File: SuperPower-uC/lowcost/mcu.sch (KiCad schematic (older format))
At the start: 0 parts

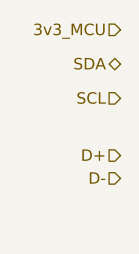
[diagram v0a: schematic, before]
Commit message: int pins and charging module
added Interrupt pins to the main sheet and finished the charging module sub sheet (with charger, fuel Gauge and power on int)
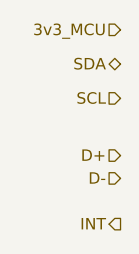
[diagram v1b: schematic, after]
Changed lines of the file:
@@
 Text HLabel 1300 1650 0    50   Input ~ 0
 D-
+Text HLabel 1300 1850 0    50   Output ~ 0
+INT
 $EndSCHEMATC

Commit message: relocated ftdi to connector sheet
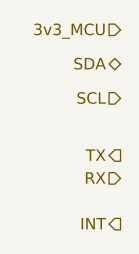
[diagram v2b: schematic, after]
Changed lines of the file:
@@
 Text HLabel 1300 1300 0    50   Input ~ 0
 SCL
-Text HLabel 1300 1550 0    50   Input ~ 0
-D+
+Text HLabel 1300 1550 0    50   Output ~ 0
+TX
 Text HLabel 1300 1650 0    50   Input ~ 0
-D-
+RX
 Text HLabel 1300 1850 0    50   Output ~ 0
 INT

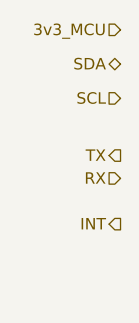
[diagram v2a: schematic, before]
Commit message: added ftdi and some cleanup
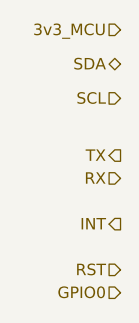
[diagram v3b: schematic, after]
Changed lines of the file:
@@
 Text HLabel 1300 1850 0    50   Output ~ 0
 INT
+Text HLabel 1300 2050 0    50   Input ~ 0
+RST
+Text HLabel 1300 2150 0    50   Input ~ 0
+GPIO0
 $EndSCHEMATC

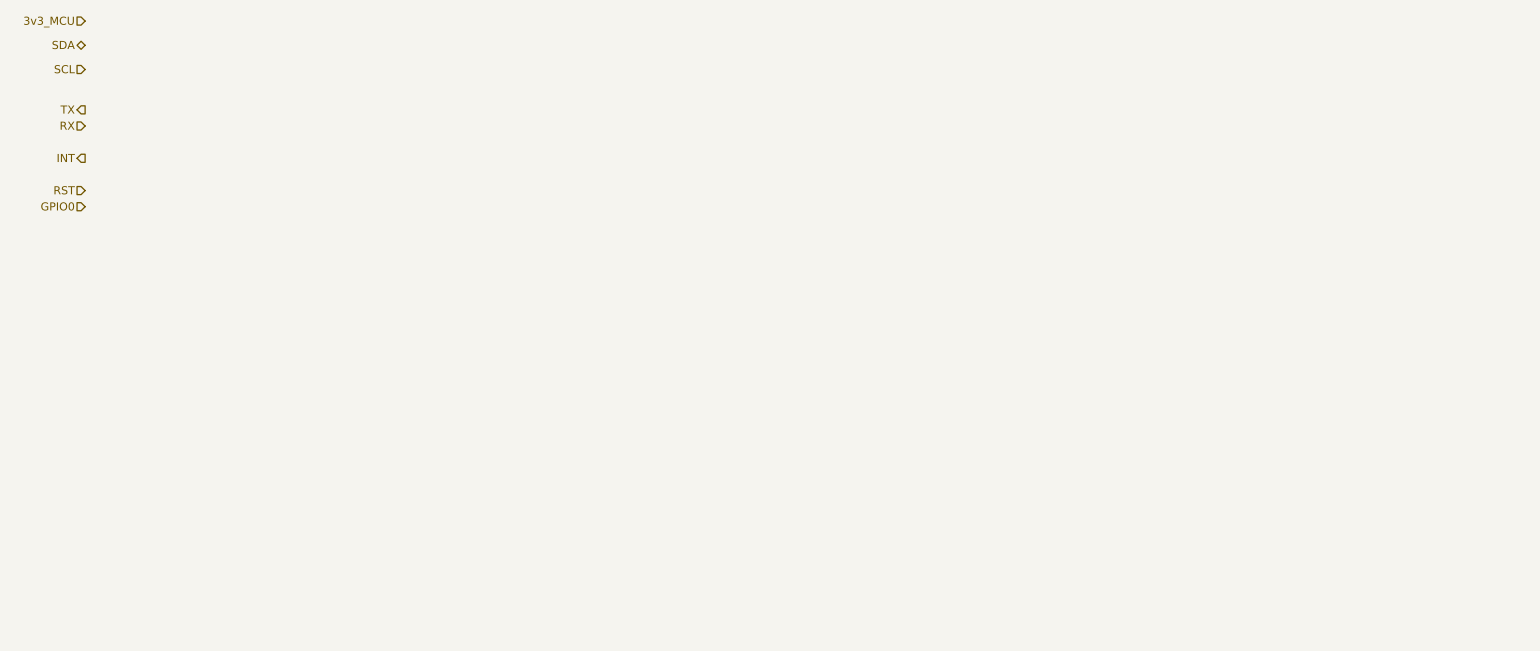
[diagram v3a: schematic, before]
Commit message: naming fixes, more components and continued schematics
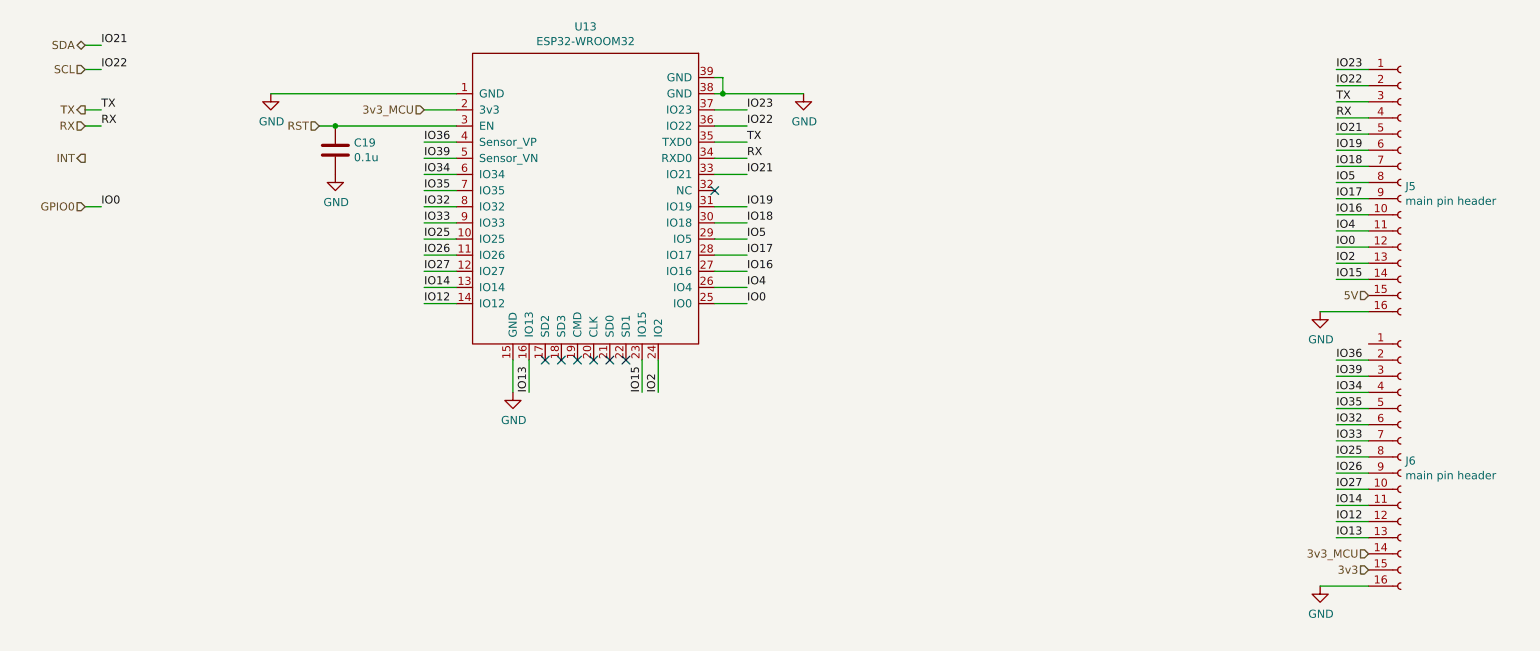
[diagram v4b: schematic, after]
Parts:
- added C19: 0.1u, Capacitor_SMD:C_0603_1608Metric_Pad1.05x0.95mm_HandSolder, symbol Device:C
- added J5, J6: main pin header, Connector_PinHeader_2.54mm:PinHeader_1x16_P2.54mm_Vertical, symbol Connector:Conn_01x16_Female
- added U13: ESP32-WROOM32, RF_Module:ESP32-WROOM-32, symbol ESP32-WROOM32:ESP32-WROOM32
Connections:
- net 3v3_MCU: now also J6.14 (Pin_14), U13.2 (3v3)
- net GPIO0: now also J5.12 (Pin_12), U13.25 (IO0)
- net RST: now also C19.1, U13.3 (EN)
- net RX: now also J5.4 (Pin_4), U13.34 (RXD0)
- net SCL: now also J5.2 (Pin_2), U13.36 (IO22)
- net SDA: now also J5.5 (Pin_5), U13.33 (IO21)
- net TX: now also J5.3 (Pin_3), U13.35 (TXD0)
- new net 3v3: J6.15 (Pin_15)
- new net 5V: J5.15 (Pin_15)
- new net GND: C19.2, J5.16 (Pin_16), J6.16 (Pin_16), U13.1 (GND), U13.15 (GND), U13.38 (GND), U13.39 (GND)
- new net IO12: J6.12 (Pin_12), U13.14 (IO12)
- new net IO13: J6.13 (Pin_13), U13.16 (IO13)
- new net IO14: J6.11 (Pin_11), U13.13 (IO14)
- new net IO15: J5.14 (Pin_14), U13.23 (IO15)
- new net IO16: J5.10 (Pin_10), U13.27 (IO16)
- new net IO17: J5.9 (Pin_9), U13.28 (IO17)
- new net IO18: J5.7 (Pin_7), U13.30 (IO18)
- new net IO19: J5.6 (Pin_6), U13.31 (IO19)
- new net IO2: J5.13 (Pin_13), U13.24 (IO2)
- new net IO23: J5.1 (Pin_1), U13.37 (IO23)
- new net IO25: J6.8 (Pin_8), U13.10 (IO25)
- new net IO26: J6.9 (Pin_9), U13.11 (IO26)
- new net IO27: J6.10 (Pin_10), U13.12 (IO27)
- new net IO32: J6.6 (Pin_6), U13.8 (IO32)
- new net IO33: J6.7 (Pin_7), U13.9 (IO33)
- new net IO34: J6.4 (Pin_4), U13.6 (IO34)
- new net IO35: J6.5 (Pin_5), U13.7 (IO35)
- new net IO36: J6.2 (Pin_2), U13.4 (Sensor_VP)
- new net IO39: J6.3 (Pin_3), U13.5 (Sensor_VN)
- new net IO4: J5.11 (Pin_11), U13.26 (IO4)
- new net IO5: J5.8 (Pin_8), U13.29 (IO5)
- no-connect marks 0 -> 7

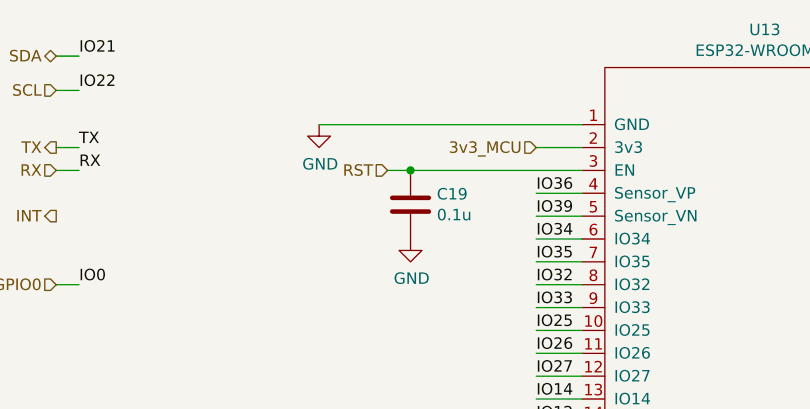
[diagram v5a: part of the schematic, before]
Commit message: started pcb and added .1u cap to mcu vcc
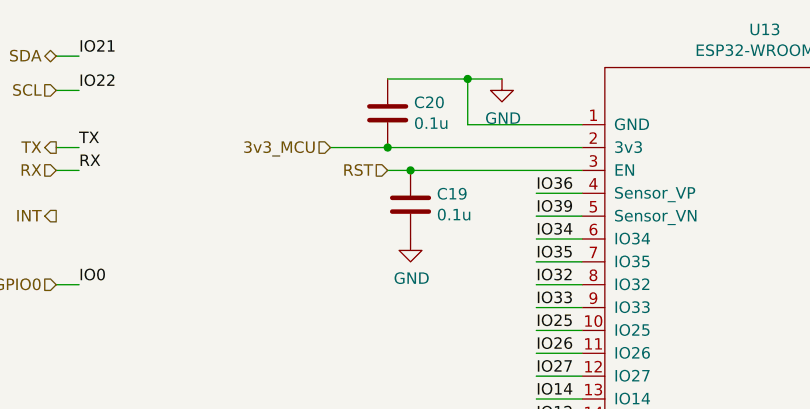
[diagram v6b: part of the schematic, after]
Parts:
- added C20: 0.1u, Capacitor_SMD:C_0603_1608Metric_Pad1.05x0.95mm_HandSolder, symbol Device:C
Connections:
- net 3v3_MCU: now also C20.2
- net GND: now also C20.1
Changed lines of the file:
@@
 Comment4 ""
 $EndDescr
-Text HLabel 3400 1550 0    50   Input ~ 0
+Text HLabel 2500 1550 0    50   Input ~ 0
 3v3_MCU
 Text HLabel 1300 1150 0    50   BiDi ~ 0
@@
 $EndComp
 Wire Wire Line
-	3600 1550 3400 1550
+	3600 1550 2750 1550
 Wire Wire Line
 	3600 1750 3400 1750
@@
 Wire Wire Line
 	5250 1450 5750 1450
-$Comp
-L power:GND #PWR0116
-U 1 1 5F8A73B4
-P 2450 1450
-F 0 "#PWR0116" H 2450 1200 50  0001 C CNN
-F 1 "GND" H 2455 1277 50  0000 C CNN
-F 2 "" H 2450 1450 50  0001 C CNN
-F 3 "" H 2450 1450 50  0001 C CNN
-	1    2450 1450
-	1    0    0    -1
-$EndComp
-Wire Wire Line
-	2450 1450 3600 1450
 Wire Wire Line
 	5400 1750 5200 1750
@@
 Text HLabel 9250 2700 0    50   Input ~ 0
 5V
+$Comp
+L Device:C C20
+U 1 1 5F818647
+P 2750 1400
+F 0 "C20" H 2865 1446 50  0000 L CNN
+F 1 "0.1u" H 2865 1355 50  0000 L CNN
+F 2 "Capacitor_SMD:C_0603_1608Metric_Pad1.05x0.95mm_HandSolder" H 2788 1250 50  0001 C CNN
+F 3 "~" H 2750 1400 50  0001 C CNN
+F 4 "C14858" H 2750 1400 50  0001 C CNN "LCSC"
+	1    2750 1400
+	1    0    0    -1
+$EndComp
+Connection ~ 2750 1550
+Wire Wire Line
+	2750 1550 2500 1550
+Wire Wire Line
+	2750 1250 3100 1250
+Wire Wire Line
+	3100 1250 3100 1450
+Wire Wire Line
+	3100 1450 3600 1450
+Wire Wire Line
+	3100 1250 3250 1250
+Connection ~ 3100 1250
+$Comp
+L power:GND #PWR?
+U 1 1 5F82BD5E
+P 3250 1250
+F 0 "#PWR?" H 3250 1000 50  0001 C CNN
+F 1 "GND" H 3255 1077 50  0000 C CNN
+F 2 "" H 3250 1250 50  0001 C CNN
+F 3 "" H 3250 1250 50  0001 C CNN
+	1    3250 1250
+	1    0    0    -1
+$EndComp
 $EndSCHEMATC

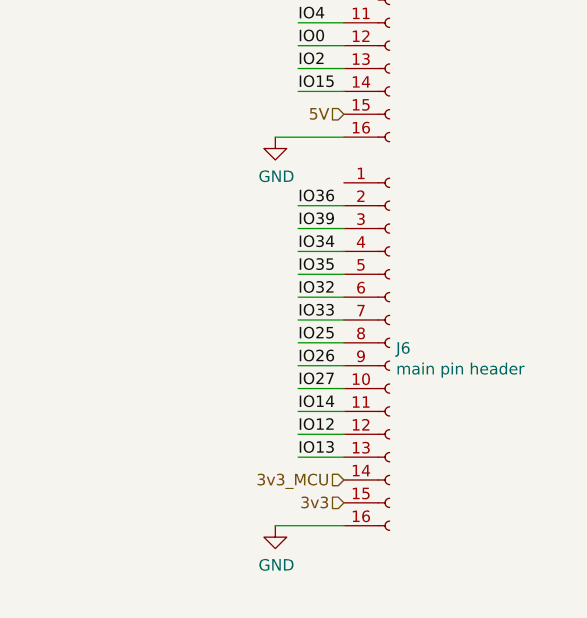
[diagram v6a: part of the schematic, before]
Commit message: fixed erc errors
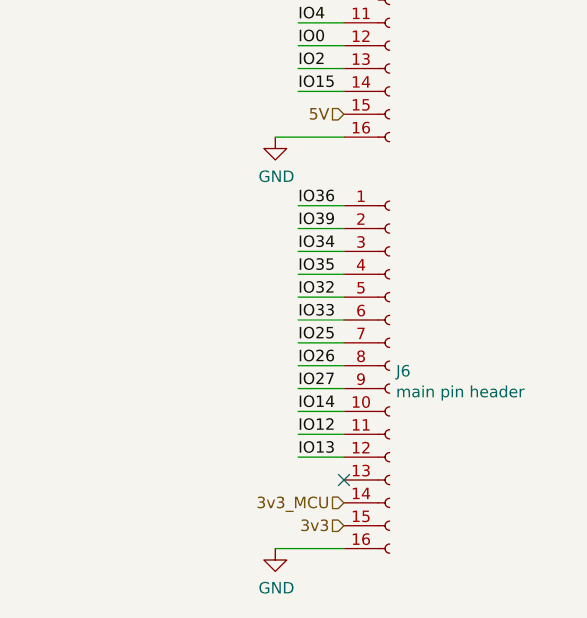
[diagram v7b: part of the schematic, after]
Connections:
- net IO12: now also J6.11 (Pin_11); no longer J6.12 (Pin_12)
- net IO13: now also J6.12 (Pin_12); no longer J6.13 (Pin_13)
- net IO14: now also J6.10 (Pin_10); no longer J6.11 (Pin_11)
- net IO25: now also J6.7 (Pin_7); no longer J6.8 (Pin_8)
- net IO26: now also J6.8 (Pin_8); no longer J6.9 (Pin_9)
- net IO27: now also J6.9 (Pin_9); no longer J6.10 (Pin_10)
- net IO32: now also J6.5 (Pin_5); no longer J6.6 (Pin_6)
- net IO33: now also J6.6 (Pin_6); no longer J6.7 (Pin_7)
- net IO34: now also J6.3 (Pin_3); no longer J6.4 (Pin_4)
- net IO35: now also J6.4 (Pin_4); no longer J6.5 (Pin_5)
- net IO36: now also J6.1 (Pin_1); no longer J6.2 (Pin_2)
- net IO39: now also J6.2 (Pin_2); no longer J6.3 (Pin_3)
- no-connect marks 7 -> 8
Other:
- moved on the sheet: J6
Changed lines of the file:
@@
 L Connector:Conn_01x16_Female J6
 U 1 1 5F896962
-P 9450 3700
-F 0 "J6" H 9478 3676 50  0000 L CNN
-F 1 "main pin header" H 9478 3585 50  0000 L CNN
-F 2 "Connector_PinHeader_2.54mm:PinHeader_1x16_P2.54mm_Vertical" H 9450 3700 50  0001 C CNN
-F 3 "~" H 9450 3700 50  0001 C CNN
-	1    9450 3700
+P 9450 3800
+F 0 "J6" H 9478 3776 50  0000 L CNN
+F 1 "main pin header" H 9478 3685 50  0000 L CNN
+F 2 "Connector_PinHeader_2.54mm:PinHeader_1x16_P2.54mm_Vertical" H 9450 3800 50  0001 C CNN
+F 3 "~" H 9450 3800 50  0001 C CNN
+	1    9450 3800
 	1    0    0    -1
 $EndComp
@@
 IO13
 Wire Wire Line
-	9250 4500 8950 4500
+	9250 4600 8950 4600
 Wire Wire Line
 	9250 2800 8950 2800
@@
 L power:GND #PWR0120
 U 1 1 5F8C9F4B
-P 8950 4500
-F 0 "#PWR0120" H 8950 4250 50  0001 C CNN
-F 1 "GND" H 8955 4327 50  0000 C CNN
-F 2 "" H 8950 4500 50  0001 C CNN
-F 3 "" H 8950 4500 50  0001 C CNN
-	1    8950 4500
+P 8950 4600
+F 0 "#PWR0120" H 8950 4350 50  0001 C CNN
+F 1 "GND" H 8955 4427 50  0000 C CNN
+F 2 "" H 8950 4600 50  0001 C CNN
+F 3 "" H 8950 4600 50  0001 C CNN
+	1    8950 4600
 	1    0    0    -1
 $EndComp
@@
 Text Label 9050 2600 0    50   ~ 0
 IO15
-Text HLabel 9250 4300 0    50   Input ~ 0
+Text HLabel 9250 4400 0    50   Input ~ 0
 3v3_MCU
-Text HLabel 9250 4400 0    50   Input ~ 0
+Text HLabel 9250 4500 0    50   Input ~ 0
 3v3
 Text HLabel 9250 2700 0    50   Input ~ 0
@@
 Connection ~ 3100 1250
 $Comp
-L power:GND #PWR?
+L power:GND #PWR0116
 U 1 1 5F82BD5E
 P 3250 1250
-F 0 "#PWR?" H 3250 1000 50  0001 C CNN
+F 0 "#PWR0116" H 3250 1000 50  0001 C CNN
 F 1 "GND" H 3255 1077 50  0000 C CNN
 F 2 "" H 3250 1250 50  0001 C CNN
@@
 	1    0    0    -1
 $EndComp
+NoConn ~ 9250 4300
 $EndSCHEMATC

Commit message: design rule optimisation
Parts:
- C19, C20: value 0.1u -> 0.1µF
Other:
- moved on the sheet: C19, C20, U13
